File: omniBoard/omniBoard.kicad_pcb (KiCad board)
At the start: 2 copper layers, 100 x 75 mm, 30 parts, among them J1 Conn_01x02, J2 Conn_01x02, J3 Conn_01x02, J4 Conn_01x04, J5 Conn_01x04, J6 Raspberry_Pi_2_3, J7 Conn_01x04, J8 Conn_01x04, U1 LM324, U2 LM2596_module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

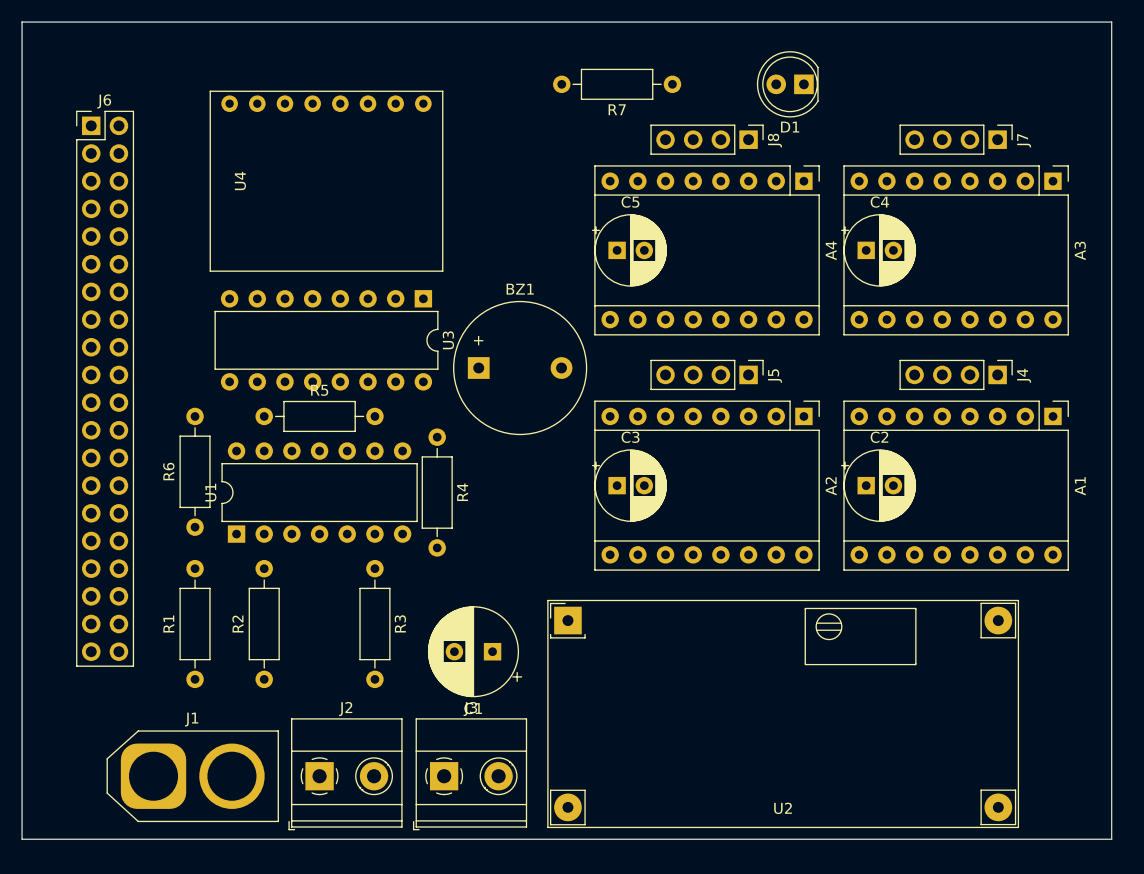
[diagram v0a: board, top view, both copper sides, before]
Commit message: Remove useless components
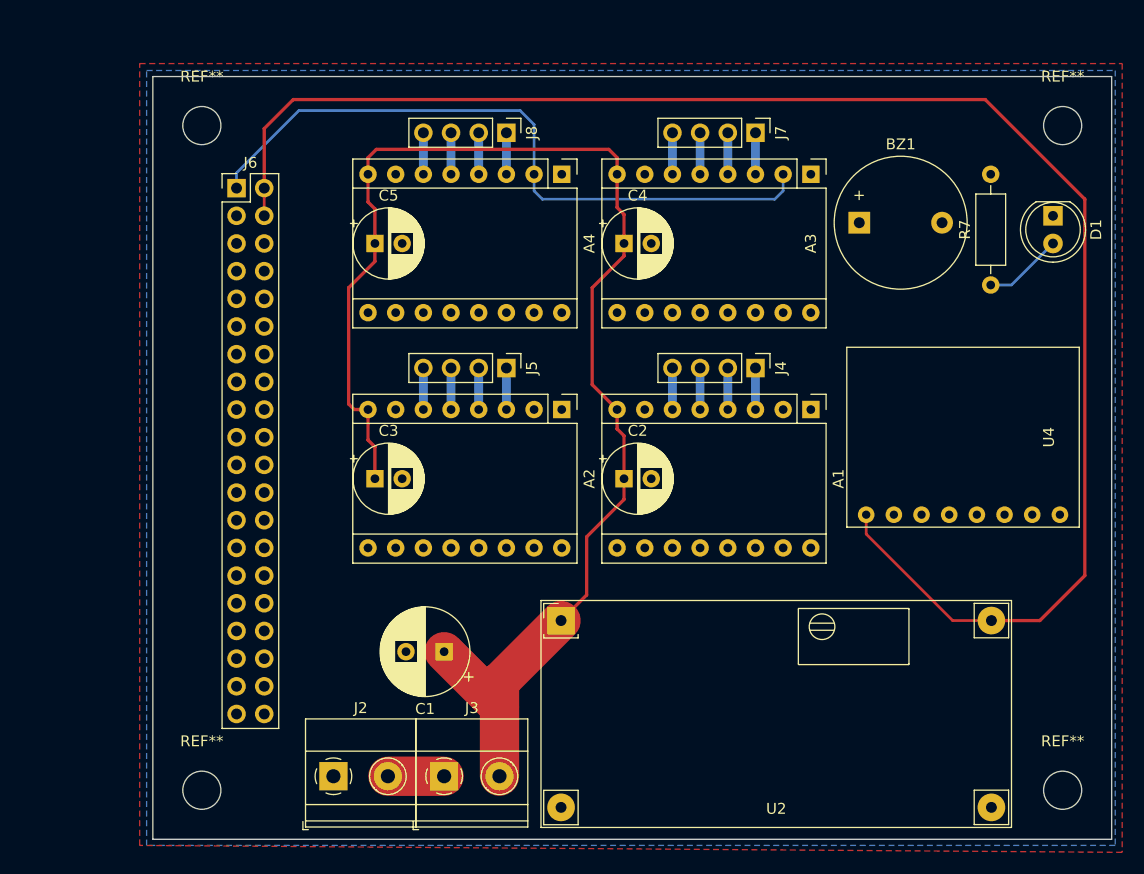
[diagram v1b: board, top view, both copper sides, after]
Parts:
- removed J1: Conn_01x02, Connector_AMASS:AMASS_XT60-F_1x02_P7.20mm_Vertical
- removed R1, R2, R3, R4, R5, R6: R, Resistor_THT:R_Axial_DIN0207_L6.3mm_D2.5mm_P10.16mm_Horizontal
- removed U1: LM324, Package_DIP:DIP-14_W7.62mm
- removed U3: 74LS147, Package_DIP:DIP-16_W7.62mm
- added REF**: MountingHole_3.5mm, MountingHole:MountingHole_3.5mm, F.Cu at (16.5, 70.5)
- added REF**: MountingHole_3.5mm, MountingHole:MountingHole_3.5mm, F.Cu at (95.5, 70.5)
- added REF**: MountingHole_3.5mm, MountingHole:MountingHole_3.5mm, F.Cu at (95.5, 9.50)
- added REF**: MountingHole_3.5mm, MountingHole:MountingHole_3.5mm, F.Cu at (16.5, 9.50)
- J3: footprint TerminalBlock_Phoenix:TerminalBlock_Phoenix_MKDS-1,5-2_1x02_P5.00mm_Horizontal -> TerminalBlock_Phoenix:TerminalBlock_Phoenix_MKDS-1,5-2-5.08_1x02_P5.08mm_Horizontal
- moved U4 63.0 mm to (86.4, 38.1), turned to 90 degrees
- moved BZ1 37.4 mm to (76.8, 18.4)
- moved R7 34.5 mm to (88.9, 24.1), turned to 90 degrees
- moved D1 25.8 mm to (94.6, 17.8), turned to 270 degrees
- moved C2 22.2 mm to (55.2, 41.9)
- moved C3 22.2 mm to (32.4, 41.9)
- moved C4 22.2 mm to (55.2, 20.3)
- moved C5 22.2 mm to (32.4, 20.3)
- moved A1 22.2 mm to (72.4, 35.6)
- moved A2 22.2 mm to (49.5, 35.6)
- moved A3 22.2 mm to (72.4, 14.0)
- moved A4 22.2 mm to (49.5, 14.0)
- moved J4 22.2 mm to (67.3, 31.8)
- moved J5 22.2 mm to (44.5, 31.8)
- moved J7 22.2 mm to (67.3, 10.2)
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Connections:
- J2 pad 1: Net-(J1-Pad2) -> GND
- J2 pad 2: GND -> Net-(J2-Pad2)
- J3 pad 1: Net-(J1-Pad2) -> Net-(J2-Pad2)
- J6 pad 1: Net-(J6-Pad1) -> +3V3
- J6 pad 17: Net-(J6-Pad17) -> +3V3
- J6 pad 2: Net-(J6-Pad2) -> +5V
- J6 pad 22: Net-(J6-Pad22) -> /M0_DIR
- J6 pad 24: Net-(J6-Pad24) -> /M1_DIR
- J6 pad 26: Net-(J6-Pad26) -> /M2_DIR
- J6 pad 28: Net-(J6-Pad28) -> /M3_DIR
- J6 pad 4: Net-(J6-Pad4) -> +5V
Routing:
- net +5V: track 0.00 -> 149.6 mm
- net +12V: track 0.00 -> 127.3 mm
- net +3V3: track 0.00 -> 62.7 mm
- net Net-(D1-Pad2): track 0.00 -> 7.29 mm
- net Net-(J2-Pad2): track 0.00 -> 5.16 mm
- net /M1_2B: track 0.00 -> 3.81 mm
- net /M1_2A: track 0.00 -> 3.81 mm
- net /M1_1B: track 0.00 -> 3.81 mm
- net /M1_1A: track 0.00 -> 3.81 mm
- net /M0_2B: track 0.00 -> 3.81 mm
- net /M0_2A: track 0.00 -> 3.81 mm
- net /M0_1B: track 0.00 -> 3.81 mm
- net /M0_1A: track 0.00 -> 3.81 mm
- net /M3_2B: track 0.00 -> 3.81 mm
- net /M3_2A: track 0.00 -> 3.81 mm
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- added copper zone on B.Cu, net GND
- added copper zone on F.Cu, net GND
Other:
- board size 100 x 75 mm -> 88 x 70 mm

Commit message: Finish board 1st version
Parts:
- moved U4 1.02 mm to (86.4, 39.1), turned to 270 degrees
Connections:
- A1 pad 10: /MS1 -> +3V3
- A1 pad 11: /MS2 -> +3V3
- A1 pad 12: /MS3 -> +3V3
- A1 pad 13: /_RESET -> /_RESET0
- A1 pad 14: /_SLEEP -> /_RESET0
- A2 pad 10: /MS1 -> +3V3
- A2 pad 11: /MS2 -> +3V3
- A2 pad 12: /MS3 -> +3V3
- A2 pad 13: /_RESET -> /_RESET1
- A2 pad 14: /_SLEEP -> /_RESET1
- A3 pad 10: /MS1 -> +3V3
- A3 pad 11: /MS2 -> +3V3
- A3 pad 12: /MS3 -> +3V3
- A3 pad 13: /_RESET -> /_RESET2
- A3 pad 14: /_SLEEP -> /_RESET2
- A4 pad 10: /MS1 -> +3V3
- A4 pad 11: /MS2 -> +3V3
- A4 pad 12: /MS3 -> +3V3
- A4 pad 13: /_RESET -> /_RESET3
- A4 pad 14: /_SLEEP -> /_RESET3
- J6 pad 11: Net-(J6-Pad11) -> /LED
- J6 pad 12: /M2_STEP -> /M3_STEP
- J6 pad 16: Net-(J6-Pad16) -> /M3_DIR
- J6 pad 22: /M0_DIR -> Net-(J6-Pad22)
- J6 pad 24: /M1_DIR -> Net-(J6-Pad24)
- J6 pad 26: /M2_DIR -> Net-(J6-Pad26)
- J6 pad 28: /M3_DIR -> Net-(J6-Pad28)
- J6 pad 31: Net-(J6-Pad31) -> /M0_DIR
- J6 pad 32: /M0_STEP -> /M2_STEP
- J6 pad 33: /M1_STEP -> /M0_STEP
- J6 pad 35: /M3_STEP -> /M1_STEP
- J6 pad 36: Net-(J6-Pad36) -> /M2_DIR
- J6 pad 38: Net-(J6-Pad38) -> /M1_DIR
- J6 pad 7: Net-(J6-Pad7) -> /BUZZER
- U4 pad 1: +5V -> +3V3
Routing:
- net /_ENABLE: track 0.00 -> 114.3 mm
- net /SCL: track 0.00 -> 95.9 mm
- net /LED: track 0.00 -> 95.8 mm
- net /SDA: track 0.00 -> 89.5 mm
- net /M2_DIR: track 0.00 -> 81.5 mm
- net /M0_DIR: track 0.00 -> 79.5 mm
- net /M2_STEP: track 0.00 -> 77.9 mm
- net /BUZZER: track 0.00 -> 77.1 mm
- net /M0_STEP: track 0.00 -> 73.7 mm
- net /M1_STEP: track 0.00 -> 47.9 mm
- net +3V3: track 62.7 -> 20.3 mm
- net GND: track 0.00 -> 41.9 mm
- net /M1_DIR: track 0.00 -> 35.4 mm
- net /M3_DIR: track 0.00 -> 31.7 mm
- net /M3_STEP: track 0.00 -> 26.3 mm
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- added copper zone on F.Cu, net +3V3
- removed copper zone on F.Cu, net GND

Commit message: Finish board 2nd version
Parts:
- added J1: Conn_01x02, TerminalBlock_Phoenix:TerminalBlock_Phoenix_MKDS-1,5-2-5.08_1x02_P5.08mm_Horizontal, F.Cu at (94.6, 64.1)
- moved C1 1.91 mm to (36.8, 57.8)
- moved J3 1.91 mm to (36.8, 69.2)
- moved U2 1.91 mm to (67.3, 63.5)
- moved J2 1.90 mm to (26.7, 69.2)
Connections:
- J6 pad 10: Net-(J6-Pad10) -> /_ENABLE
- J6 pad 2: +5V -> Net-(J6-Pad2)
- J6 pad 4: +5V -> Net-(J6-Pad4)
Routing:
- net +3V3: track 20.3 -> 192.9 mm
- net +5V: track 133.0 -> 9.27 mm
- net /_ENABLE: track 114.3 -> 123.8 mm
- net +12V: track 127.3 -> 121.9 mm
- removed copper zone on F.Cu, net +3V3

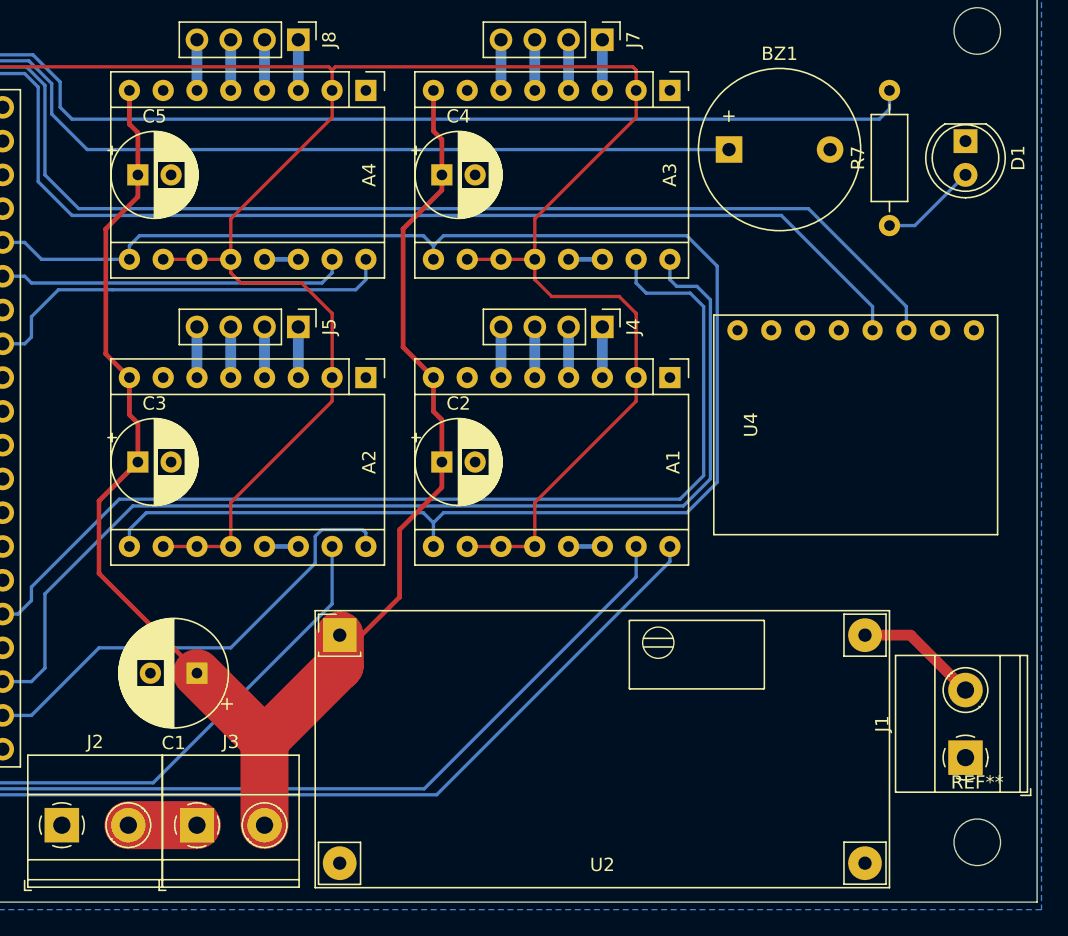
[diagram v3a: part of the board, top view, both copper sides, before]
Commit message: Add new led
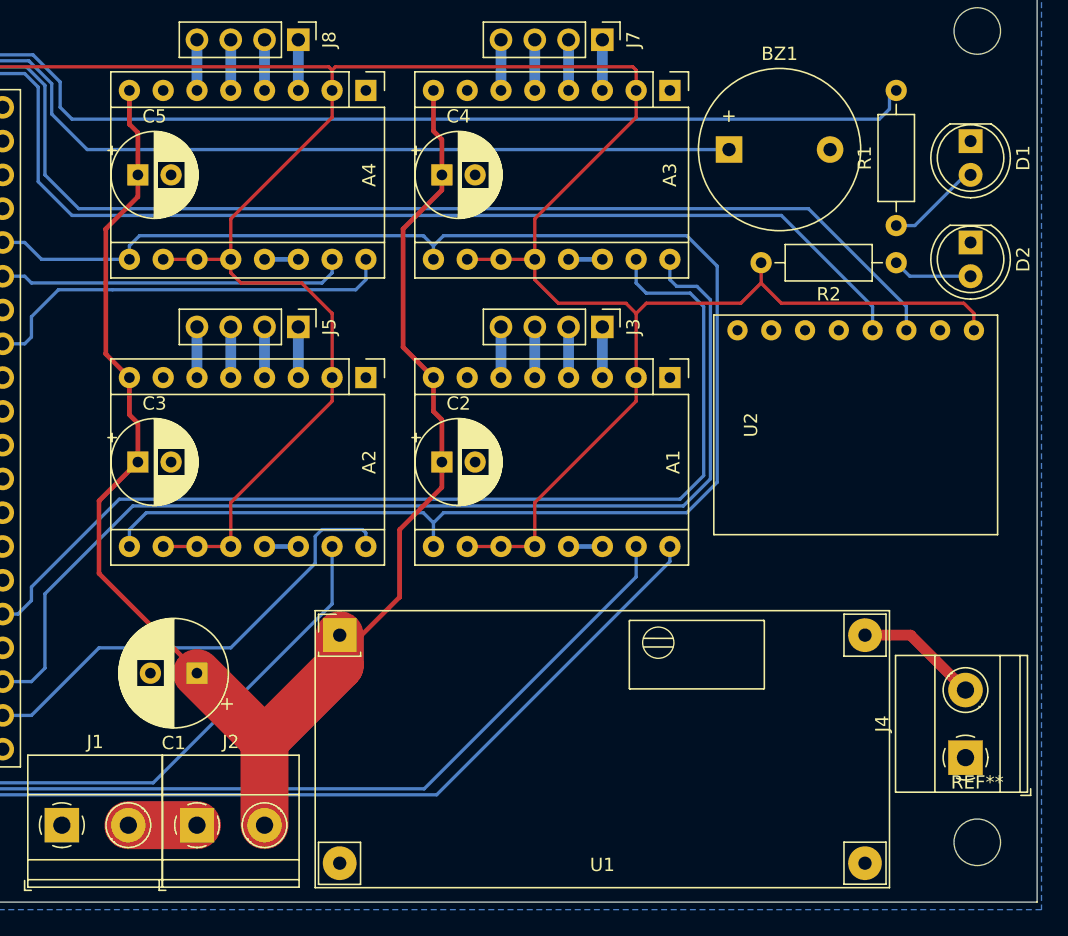
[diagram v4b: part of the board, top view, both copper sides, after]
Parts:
- added D2: LED, LED_THT:LED_D5.0mm, F.Cu at (95.0, 25.4)
- added R2: 68, Resistor_THT:R_Axial_DIN0207_L6.3mm_D2.5mm_P10.16mm_Horizontal, F.Cu at (89.4, 26.9)
- R1: renamed from R7; value 330 -> 68
- moved R1 0.51 mm to (89.4, 24.1)
- moved D1 0.38 mm to (95.0, 17.8)
- renumbered J2 to J1, J3 to J2, J4 to J3, J1 to J4, U2 to U1, U4 to U2
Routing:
- net +3V3: track 192.9 -> 223.0 mm
- net Net-(D2-Pad2): track 0.00 -> 6.01 mm

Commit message: Final version
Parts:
- removed J1: Conn_01x02, TerminalBlock_Phoenix:TerminalBlock_Phoenix_MKDS-1,5-2_1x02_P5.00mm_Horizontal
- removed J2, J4: Conn_01x02, TerminalBlock_Phoenix:TerminalBlock_Phoenix_MKDS-1,5-2-5.08_1x02_P5.08mm_Horizontal
- removed J3, J5, J7, J8: Conn_01x04, Connector_PinHeader_2.54mm:PinHeader_1x04_P2.54mm_Vertical
- removed the REF** at (16.5, 70.5)
- removed the REF** at (95.5, 70.5)
- removed the REF** at (95.5, 9.50)
- removed the REF** at (16.5, 9.50)
- removed U1: LM2596_module, omniBoard:LM2596_module
- removed U2: MPU6050_module, omniBoard:MPU6050_module
- added LM2596: LM2596_module, omniBoard:LM2596_module, F.Cu at (161.3, 116.8)
- added M1: Conn_01x04, Connector_PinHeader_2.54mm:PinHeader_1x04_P2.54mm_Vertical, F.Cu at (161.3, 85.1)
- added M2: Conn_01x04, Connector_PinHeader_2.54mm:PinHeader_1x04_P2.54mm_Vertical, F.Cu at (138.4, 85.1)
- added M3: Conn_01x04, Connector_PinHeader_2.54mm:PinHeader_1x04_P2.54mm_Vertical, F.Cu at (161.3, 63.5)
- added M4: Conn_01x04, Connector_PinHeader_2.54mm:PinHeader_1x04_P2.54mm_Vertical, F.Cu at (138.4, 63.5)
- added MPU6050: MPU6050_module, omniBoard:MPU6050_module, F.Cu at (180.3, 92.5)
- added POWER IN: Conn_01x02, TerminalBlock_Phoenix:TerminalBlock_Phoenix_MKDS-1,5-2_1x02_P5.00mm_Horizontal, F.Cu at (120.7, 122.6)
- added RASP POUT: Conn_01x02, TerminalBlock_Phoenix:TerminalBlock_Phoenix_MKDS-1,5-2-5.08_1x02_P5.08mm_Horizontal, F.Cu at (188.6, 116.8)
- added REF**: MountingHole_3.5mm, MountingHole:MountingHole_3.5mm, F.Cu at (110.5, 123.8)
- added REF**: MountingHole_3.5mm, MountingHole:MountingHole_3.5mm, F.Cu at (189.5, 123.8)
- added REF**: MountingHole_3.5mm, MountingHole:MountingHole_3.5mm, F.Cu at (189.5, 62.8)
- added REF**: MountingHole_3.5mm, MountingHole:MountingHole_3.5mm, F.Cu at (110.5, 62.8)
- added SWITCH: Conn_01x02, TerminalBlock_Phoenix:TerminalBlock_Phoenix_MKDS-1,5-2-5.08_1x02_P5.08mm_Horizontal, F.Cu at (130.8, 122.6)
- J6: value Raspberry_Pi_2_3 -> Raspberry Pi
- moved A1 108.1 mm to (166.4, 88.9)
- moved A3 108.1 mm to (166.4, 67.3)
- moved BZ1 108.1 mm to (170.8, 71.8)
- moved C1 108.1 mm to (130.8, 111.1)
- moved D1 108.1 mm to (189.0, 71.1)
- moved D2 108.1 mm to (189.0, 78.7)
- moved J6 108.1 mm to (113.7, 68.6)
- moved R1 108.1 mm to (183.4, 77.5)
- moved R2 108.1 mm to (183.4, 80.3)
- moved A2 108.1 mm to (143.5, 88.9)
- moved A4 108.1 mm to (143.5, 67.3)
- moved C2 108.1 mm to (149.2, 95.2)
- moved C3 108.1 mm to (126.4, 95.2)
- moved C4 108.1 mm to (149.2, 73.7)
- moved C5 108.1 mm to (126.4, 73.7)
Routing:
- net /M1_STEP: track 47.9 -> 47.3 mm
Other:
- board text added: "+"
- board text added: "-"
- board text added: "omniBoard"
